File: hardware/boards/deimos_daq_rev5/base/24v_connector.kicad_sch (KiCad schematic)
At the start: 14 parts, among them IC8001 INA826AIDR, J8001 Barrel_Jack PJ-202BH, U4001 INA181A2

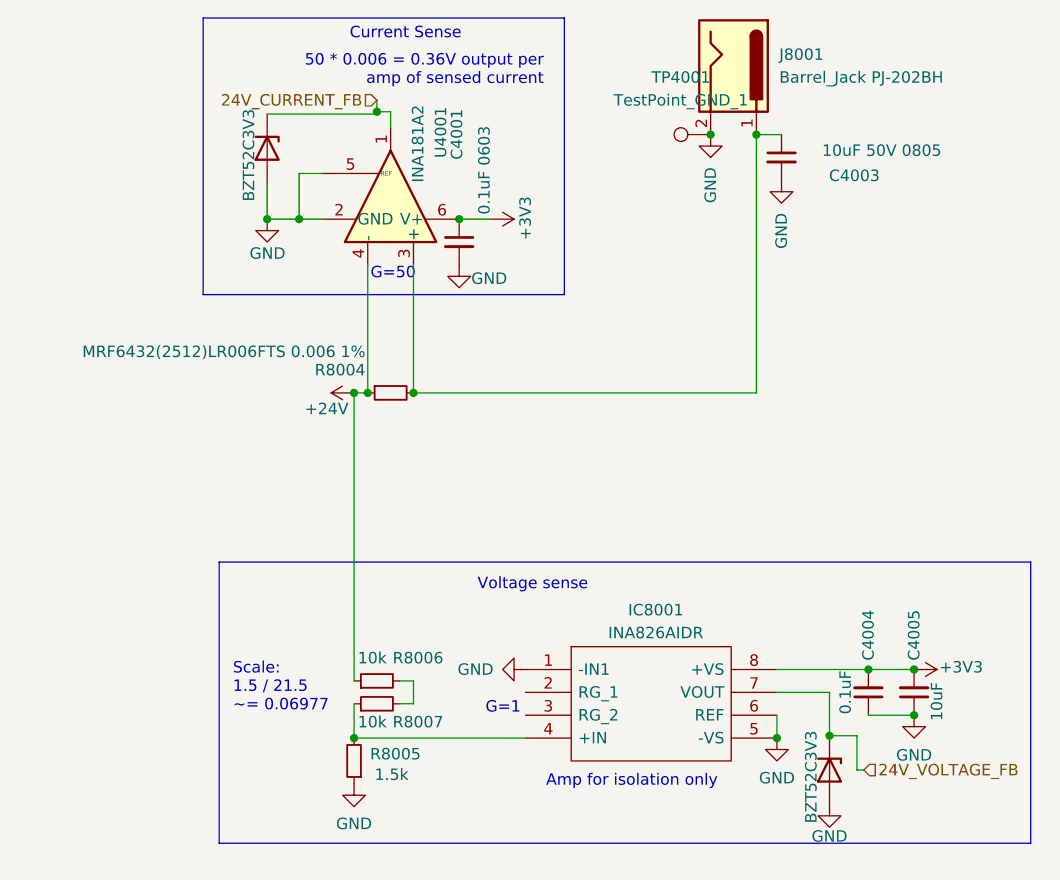
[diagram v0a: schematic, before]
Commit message: use opa196 with split rail instead of opa333 with single rail. replace zeners.
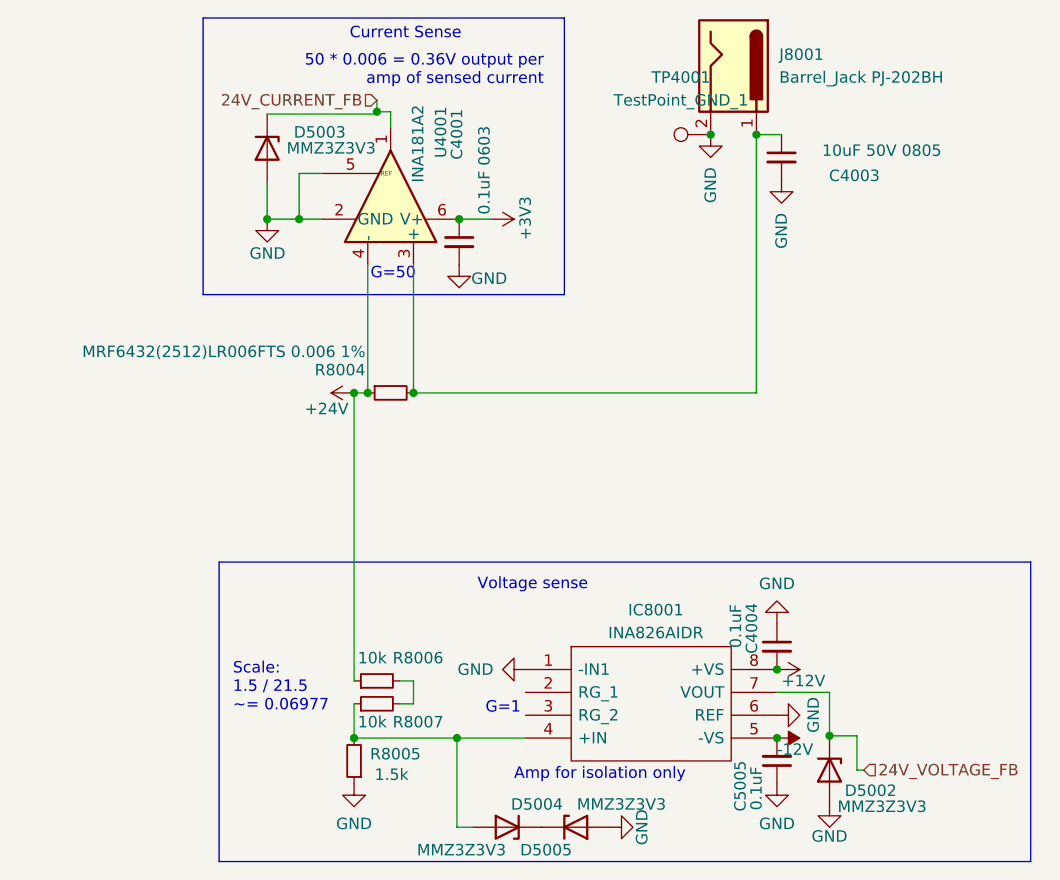
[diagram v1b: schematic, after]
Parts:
- removed C4005: 10uF, Capacitor_SMD:C_0603_1608Metric, symbol Device:C_Small
- added C5005: 0.1uF, Capacitor_SMD:C_0402_1005Metric, symbol Device:C_Small
- added D5004, D5005: MMZ3Z3V3, Diode_SMD:D_SOD-323, symbol Device:D_Zener
- D5002, D5003: value BZT52C3V3 -> MMZ3Z3V3; LCSC C2112 -> C52056
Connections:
- net +3V3: no longer C4004.2, IC8001.8 (+VS)
- net GND: now also C5005.1, D5004.2 (A); no longer IC8001.5 (-VS)
- net at IC8001.4 (+IN), R8005.2, R8007.1: now also D5005.2 (A)
- new net: D5004.1 (K), D5005.1 (K)
- new net +12V: C4004.2, IC8001.8 (+VS)
- new net -12V: C5005.2, IC8001.5 (-VS)
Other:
- moved on the sheet: C4004

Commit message: restore rev5 and make this rev rev6
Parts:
- removed C5005: 0.1uF, Capacitor_SMD:C_0402_1005Metric, symbol Device:C_Small
- removed D5004, D5005: MMZ3Z3V3, Diode_SMD:D_SOD-323, symbol Device:D_Zener
- added C4005: 10uF, Capacitor_SMD:C_0603_1608Metric, symbol Device:C_Small
- D5002, D5003: value MMZ3Z3V3 -> BZT52C3V3; LCSC C52056 -> C2112
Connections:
- net +12V is gone; now on net +3V3: C4004.2, IC8001.8 (+VS)
- net -12V is gone; now on net GND: IC8001.5 (-VS)
- net +3V3: now also C4005.2
- net GND: now also C4005.1
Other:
- moved on the sheet: C4004
